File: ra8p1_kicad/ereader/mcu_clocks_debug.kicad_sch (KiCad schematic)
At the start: 21 parts, among them J1 Cortex Debug 10-pin, U1 R7KA8P1KFLCAC#UC0, U2 TPS389001DSET, Y1 24MHz, Y2 32.768kHz

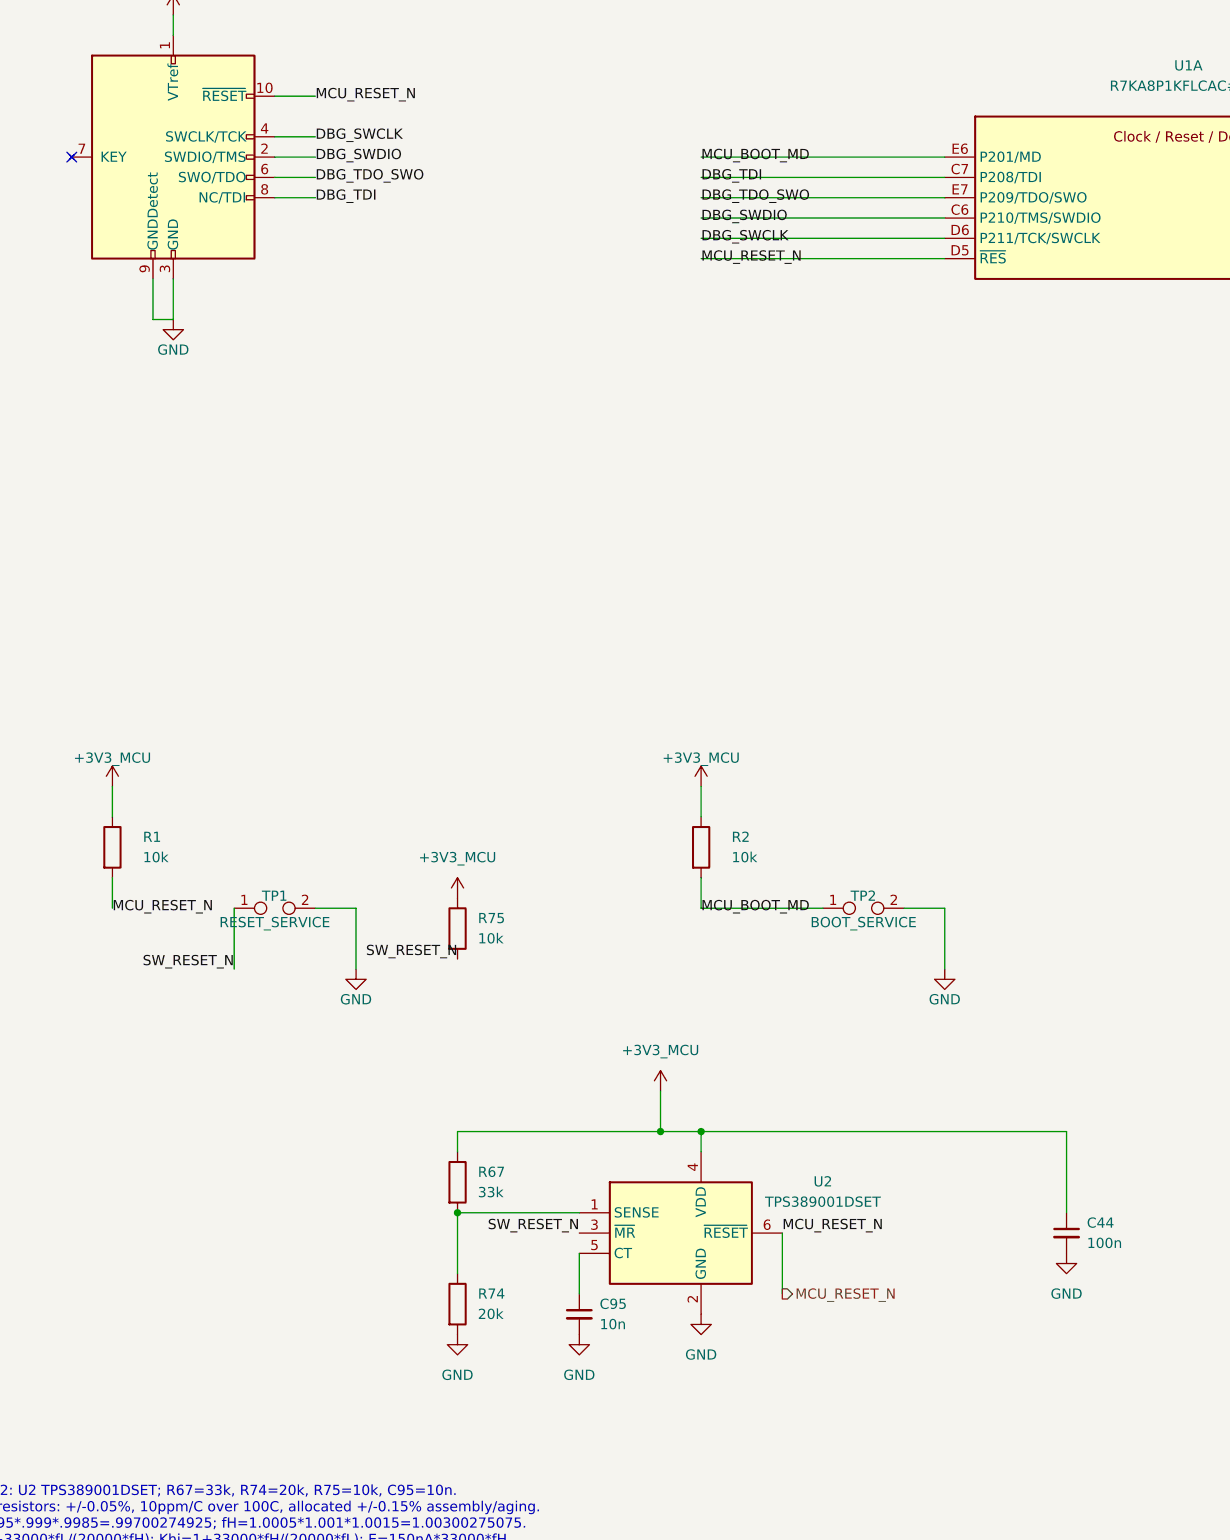
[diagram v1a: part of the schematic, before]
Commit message: wip(hardware): preserve schematic cleanup and CEU host ports
Checkpoint cosmetic cleanup across the schematic hierarchy and eleven parallel-camera host ports. Refresh the complete 13-page PDF. All 334 existing net partitions and 271 component records match the prior CEU checkpoint; all 128 ERC identities remain unchanged. Electrical design is incomplete; this is a WIP checkpoint for #821 and #841.
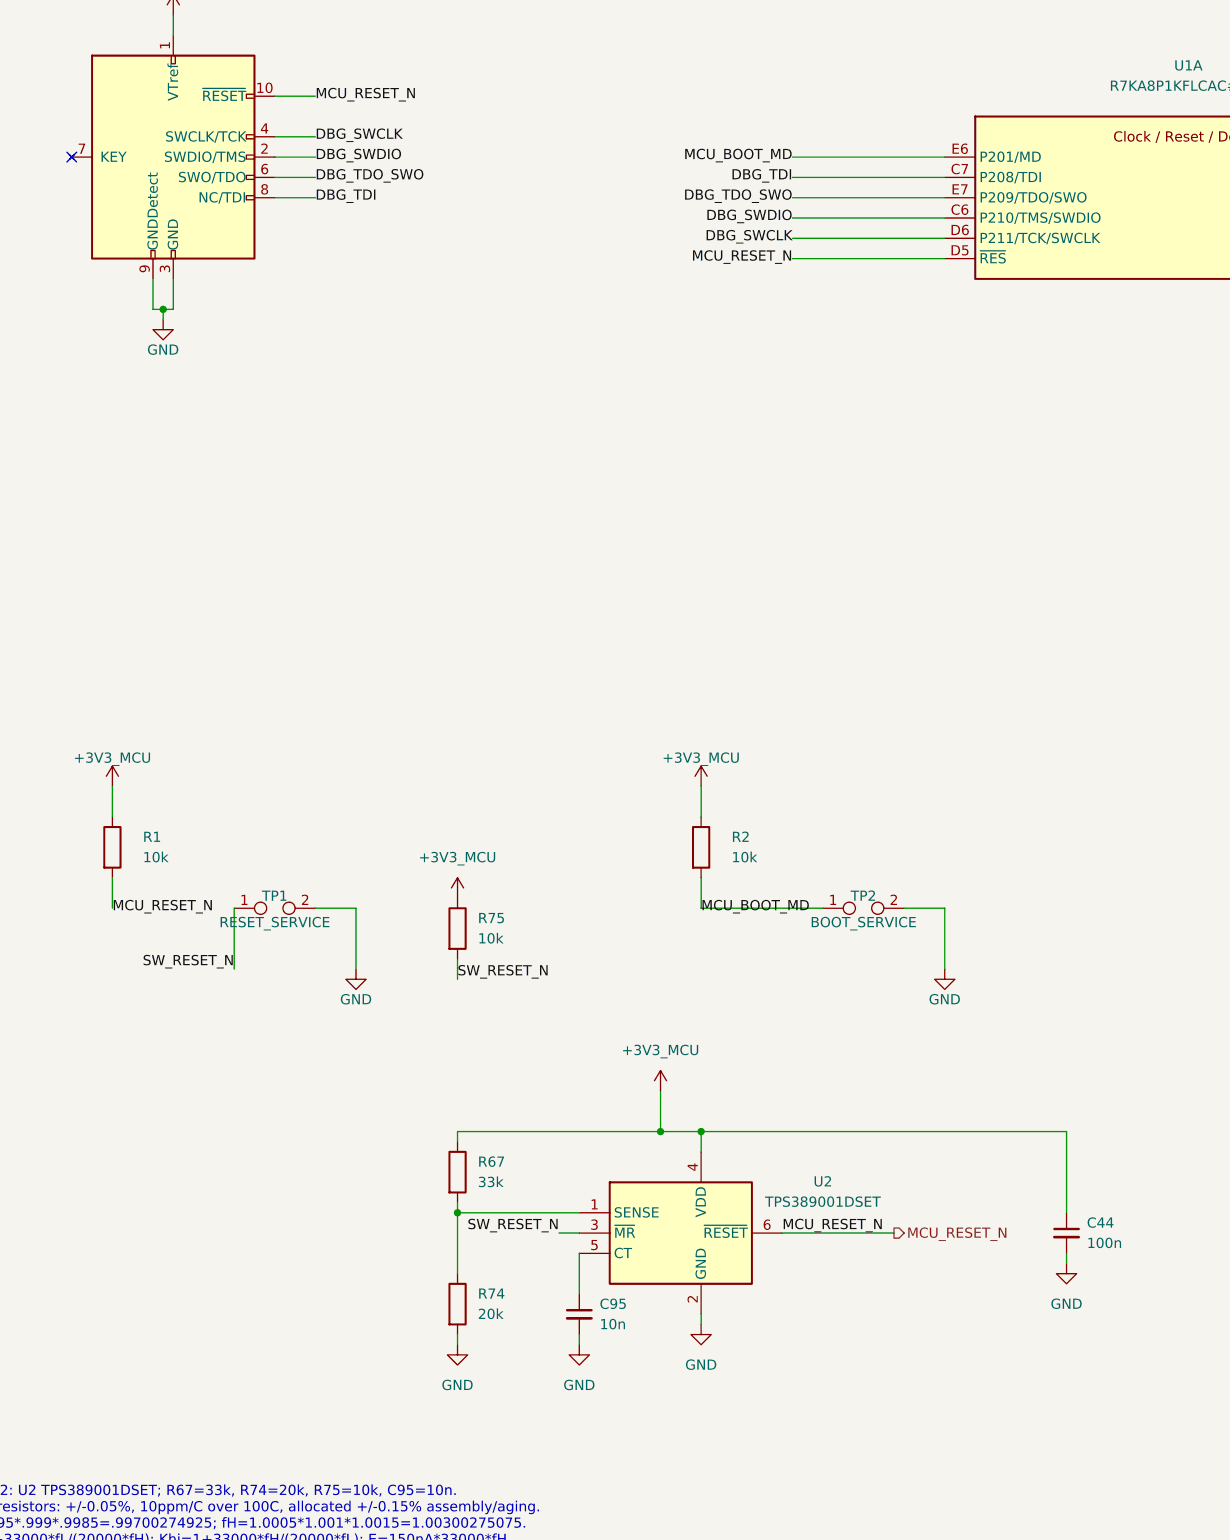
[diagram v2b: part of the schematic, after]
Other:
- moved on the sheet: R67
